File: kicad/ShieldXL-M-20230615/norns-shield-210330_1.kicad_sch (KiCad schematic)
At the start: 43 parts, among them J1 NRJ6HF, J2 NRJ6HF, J4 NRJ6HF, J5 NRJ6HF, Q1 ASFL1-12.288MHZ-LCS-T, U1 CS4270, U11 TPS793475DBVR, X1 RASPI_BOARD_B+#_E3

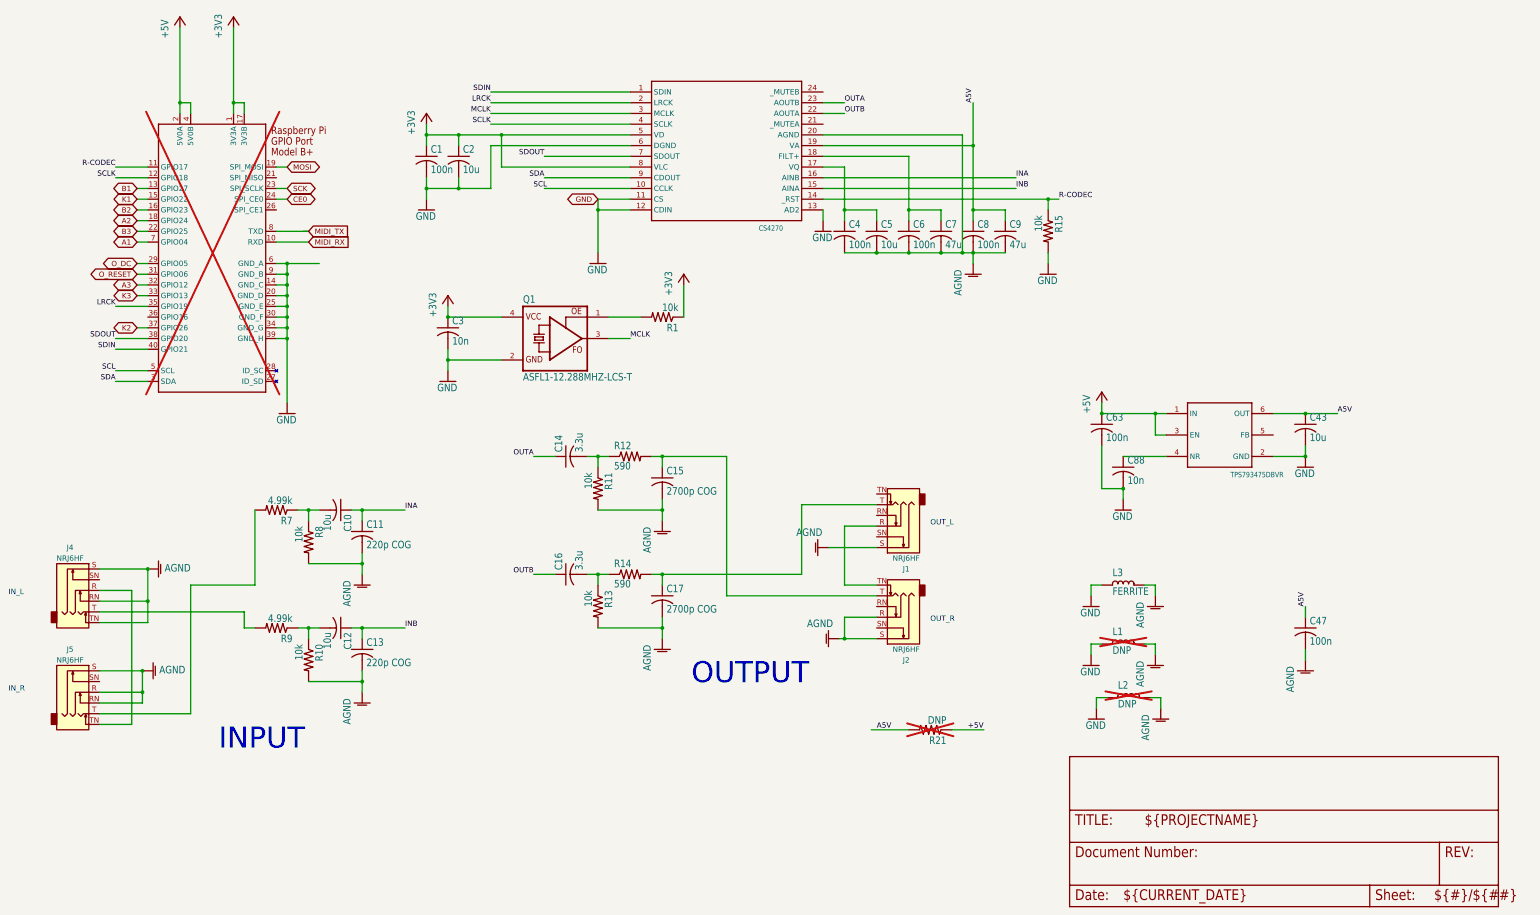
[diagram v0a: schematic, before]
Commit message: updating JLCPCB codes
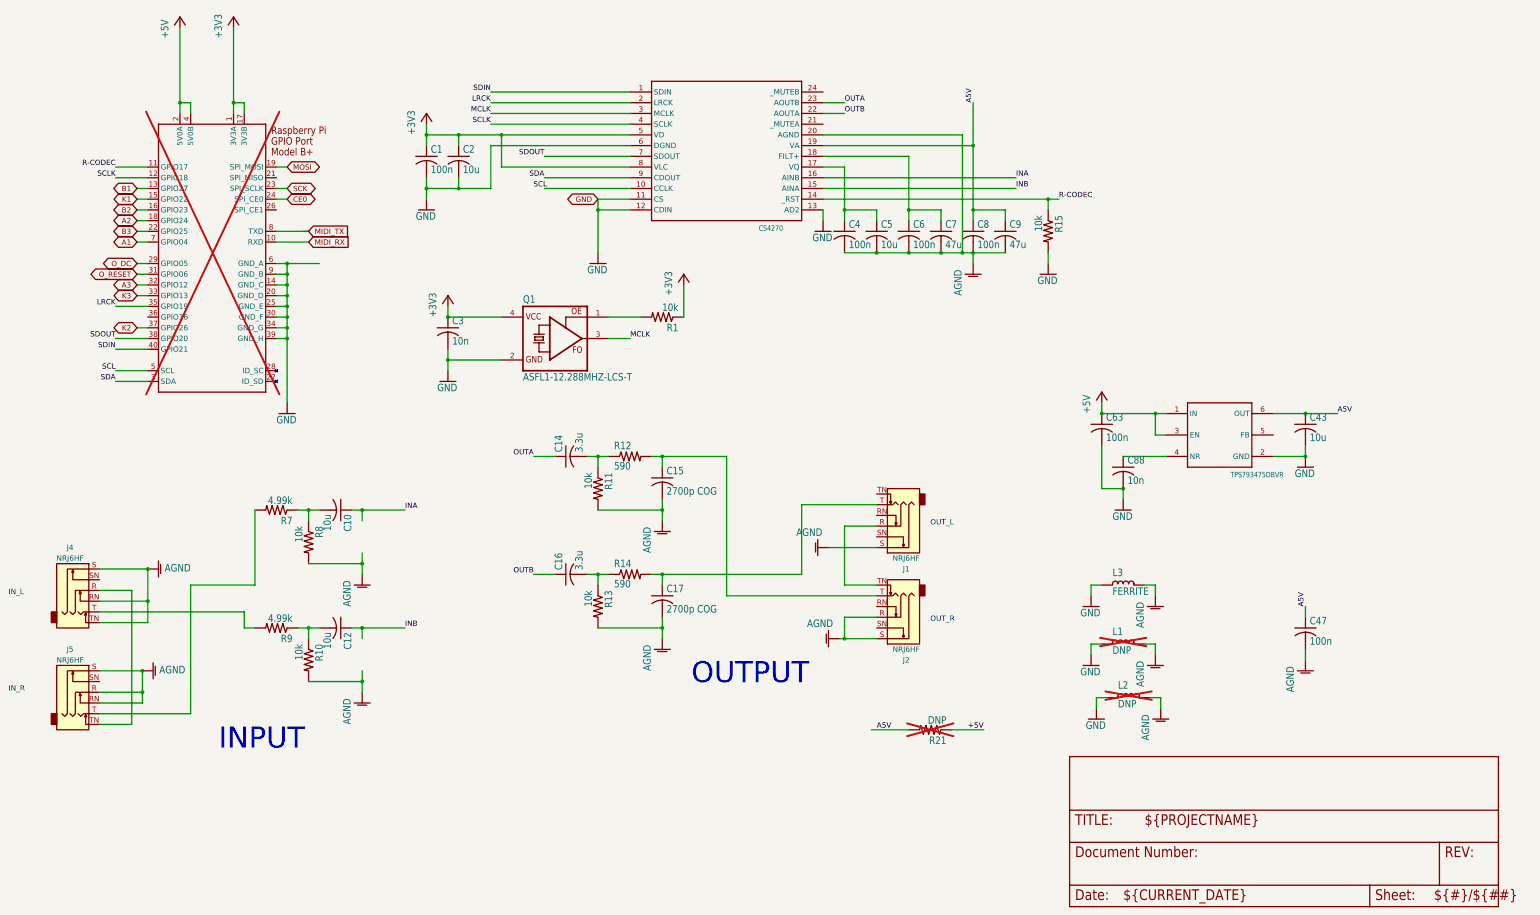
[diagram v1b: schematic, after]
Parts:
- removed C11, C13: 220p COG, ShieldXL:C0603, symbol norns-shield-210330-eagle-import:C-USC0603
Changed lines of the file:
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@@
 (kicad_sch
-	(version 20231120)
+	(version 20250114)
 	(generator "eeschema")
-	(generator_version "8.0")
+	(generator_version "9.0")
 	(paper "User" 443.23 305.206)
+	(text "OUTPUT"
+		(exclude_from_sim no)
+		(at 227.838 232.156 0)
+		(effects
+			(font
+				(size 5 5)
+			)
+			(justify left bottom)
+		)
+	)
+	(text "IN_R\n"
+		(exclude_from_sim no)
+		(at 66.04 233.68 0)
+		(effects
+			(font
+				(size 1.27 1.27)
+			)
+			(justify left bottom)
+		)
+	)
+	(text "INPUT"
+		(exclude_from_sim no)
+		(at 115.824 247.65 0)
+		(effects
+			(font
+				(size 5 5)
+			)
+			(justify left bottom)
+		)
+	)
+	(text "OUT_L"
+		(exclude_from_sim no)
+		(at 284.48 194.31 0)
+		(effects
+			(font
+				(size 1.27 1.27)
+			)
+			(justify left bottom)
+		)
+	)
+	(text "IN_L\n"
+		(exclude_from_sim no)
+		(at 66.04 210.82 0)
+		(effects
+			(font
+				(size 1.27 1.27)
+			)
+			(justify left bottom)
+		)
+	)
+	(text "OUT_R\n"
+		(exclude_from_sim no)
+		(at 284.48 217.17 0)
+		(effects
+			(font
+				(size 1.27 1.27)
+			)
+			(justify left bottom)
+		)
+	)
 	(junction
 		(at 220.98 205.74)
@@
 		)
 	)
-	(text "OUTPUT"
-		(exclude_from_sim no)
-		(at 227.838 232.156 0)
-		(effects
-			(font
-				(size 5 5)
-			)
-			(justify left bottom)
-		)
-	)
-	(text "IN_R\n"
-		(exclude_from_sim no)
-		(at 66.04 233.68 0)
-		(effects
-			(font
-				(size 1.27 1.27)
-			)
-			(justify left bottom)
-		)
-	)
-	(text "INPUT"
-		(exclude_from_sim no)
-		(at 115.824 247.65 0)
-		(effects
-			(font
-				(size 5 5)
-			)
-			(justify left bottom)
-		)
-	)
-	(text "OUT_L"
-		(exclude_from_sim no)
-		(at 284.48 194.31 0)
-		(effects
-			(font
-				(size 1.27 1.27)
-			)
-			(justify left bottom)
-		)
-	)
-	(text "IN_L\n"
-		(exclude_from_sim no)
-		(at 66.04 210.82 0)
-		(effects
-			(font
-				(size 1.27 1.27)
-			)
-			(justify left bottom)
-		)
-	)
-	(text "OUT_R\n"
-		(exclude_from_sim no)
-		(at 284.48 217.17 0)
-		(effects
-			(font
-				(size 1.27 1.27)
-			)
-			(justify left bottom)
-		)
-	)
 	(label "SCLK"
 		(at 91.44 111.76 180)
@@
 	)
 	(symbol
-		(lib_id "norns-shield-210330-eagle-import:C-USC0603")
-		(at 149.86 223.52 0)
-		(unit 1)
-		(exclude_from_sim no)
-		(in_bom yes)
-		(on_board yes)
-		(dnp no)
-		(property "Reference" "C13"
-			(at 150.876 222.885 0)
-			(effects
-				(font
-					(size 1.778 1.5113)
-				)
-				(justify left bottom)
-			)
-		)
-		(property "Value" "220p COG"
-			(at 150.876 227.711 0)
-			(effects
-				(font
-					(size 1.778 1.5113)
-				)
-				(justify left bottom)
-			)
-		)
-		(property "Footprint" "ShieldXL:C0603"
-			(at 149.86 223.52 0)
-			(effects
-				(font
-					(size 1.27 1.27)
-				)
-				(hide yes)
-			)
-		)
-		(property "Datasheet" ""
-			(at 149.86 223.52 0)
-			(effects
-				(font
-					(size 1.27 1.27)
-				)
-				(hide yes)
-			)
-		)
-		(property "Description" ""
-			(at 149.86 223.52 0)
-			(effects
-				(font
-					(size 1.27 1.27)
-				)
-				(hide yes)
-			)
-		)
-		(pin "1"
-		)
-		(pin "2"
-		)
-		(instances
-			(project "ShieldXL-M"
-				(path "/b86e8947-58dc-49c6-bb5d-ce6d33c2e465/d872c92c-5229-43e6-807a-8bd0f3dfa8f7"
-					(reference "C13")
-					(unit 1)
-				)
-			)
-		)
-	)
-	(symbol
 		(lib_id "norns-shield-210330-eagle-import:R-US_R0603")
 		(at 284.48 242.57 180)
@@
 					(unit 1)
 				)
-			)
-		)
-	)
-	(symbol
-		(lib_id "norns-shield-210330-eagle-import:C-USC0603")
-		(at 149.86 195.58 0)
-		(unit 1)
-		(exclude_from_sim no)
-		(in_bom yes)
-		(on_board yes)
-		(dnp no)
-		(property "Reference" "C11"
-			(at 150.876 194.945 0)
-			(effects
-				(font
-					(size 1.778 1.5113)
-				)
-				(justify left bottom)
-			)
-		)
-		(property "Value" "220p COG"
-			(at 150.876 199.771 0)
-			(effects
-				(font
-					(size 1.778 1.5113)
-				)
-				(justify left bottom)
-			)
-		)
-		(property "Footprint" "ShieldXL:C0603"
-			(at 149.86 195.58 0)
-			(effects
-				(font
-					(size 1.27 1.27)
-				)
-				(hide yes)
-			)
-		)
-		(property "Datasheet" ""
-			(at 149.86 195.58 0)
-			(effects
-				(font
-					(size 1.27 1.27)
-				)
-				(hide yes)
-			)
-		)
-		(property "Description" ""
-			(at 149.86 195.58 0)
-			(effects
-				(font
-					(size 1.27 1.27)
-				)
-				(hide yes)
-			)
-		)
-		(pin "1"
-		)
-		(pin "2"
-		)
-		(instances
-			(project "ShieldXL-M"
-				(path "/b86e8947-58dc-49c6-bb5d-ce6d33c2e465/d872c92c-5229-43e6-807a-8bd0f3dfa8f7"
-					(reference "C11")
-					(unit 1)
-				)
